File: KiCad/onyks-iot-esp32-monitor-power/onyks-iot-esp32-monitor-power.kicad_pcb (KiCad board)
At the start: 2 copper layers, 54.9 x 72.1 mm, 54 parts, among them J1 Uart_con, J10 PAD, J11 PAD, J12 PAD, J13 PAD, J14 +3V3_PAD, J15 +5V_PAD, J16 FOUT_conn, J17 Ground, J2 Jtag_con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

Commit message: fab files v1
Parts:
- added C9: 10u, Capacitor_SMD:C_0805_2012Metric, F.Cu at (160.1, 71.1)
- added D4: D_Zener, Diode_SMD:D_0805_2012Metric, F.Cu at (156.5, 73.4)
- added D5: D_Zener, Diode_SMD:D_0805_2012Metric, F.Cu at (152.9, 73.4)
- added R2: calc, Resistor_SMD:R_0805_2012Metric, F.Cu at (157.7, 67.1)
- added R3: calc, Resistor_SMD:R_0805_2012Metric, F.Cu at (157.7, 69.1)
- added R4: 1k, Resistor_SMD:R_0805_2012Metric, F.Cu at (156.4, 71.1)
- C1, C4, C6: value 100n -> 100n/10V
- C2: value 10u -> 10u/10V
- C3: value 1u -> 1u/10V
- C5: value 1n -> 1n/10V
- C7, C8: value 10u -> 10u/25V
- T1: value Transformer_1P_1S -> 2mA-2mA transformer
- moved J10 6.10 mm to (157.7, 64.4)
- moved J11 5.91 mm to (158.8, 62.5)
- moved J5 0.08 mm to (177.0, 106.3)
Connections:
- net SCL renamed /SCL
- net SDA renamed /SDA
- R10 pad 1: /A1 -> Net-(T1-SB)
- T1 pad 4: /A1 -> Net-(T1-SB)
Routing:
- net +3V3: track 199.0 -> 210.3 mm
- net Net-(T1-SB): track 0.00 -> 8.47 mm
- net /A1: track 20.2 -> 16.0 mm
- net /A0: track 35.6 -> 33.4 mm
- net /EN: track 99.6 -> 101.5 mm
- net Net-(C9-Pad2): track 0.00 -> 1.78 mm
- net Net-(D4-K): track 0.00 -> 1.78 mm
- net /SDA: track 40.4 -> 38.7 mm
- net /SCL: track 42.8 -> 41.2 mm
- net GND: vias 123 -> 70
- net Earth: vias 132 -> 55
- net (no net): vias 0 -> 3
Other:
- board text added: "ONYKS iot esp32 moitor power V1"
- board text removed: "ONYKS iot esp32 moitor power"

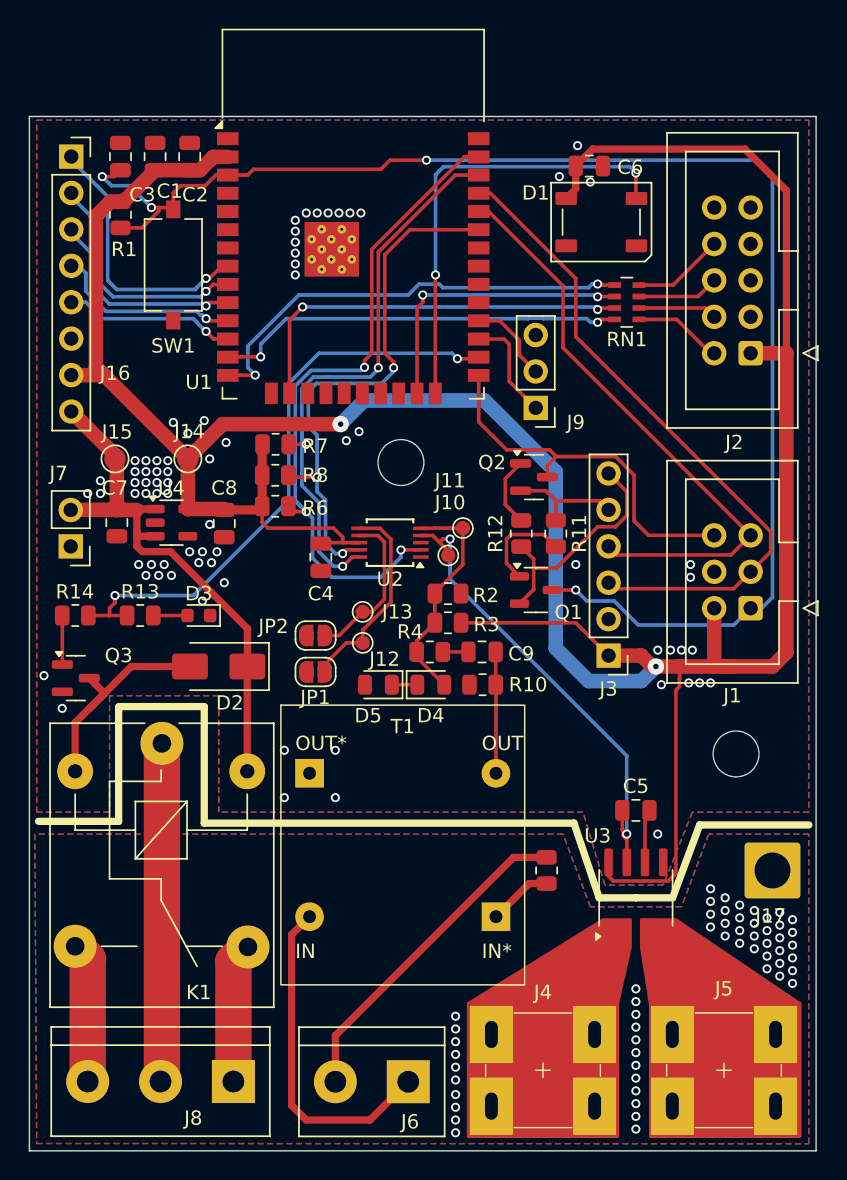
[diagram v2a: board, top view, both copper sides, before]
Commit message: vias 31mils
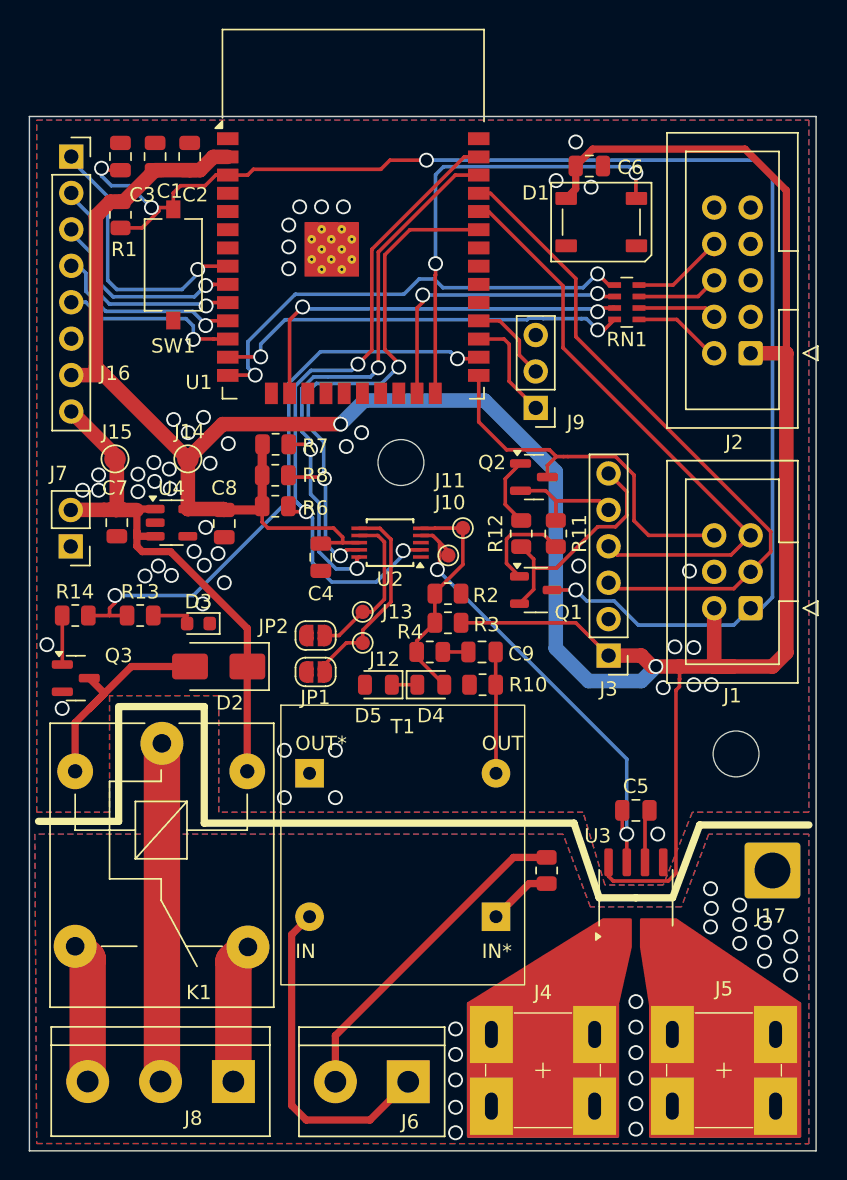
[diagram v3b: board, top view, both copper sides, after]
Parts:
- moved D3 0.56 mm to (140.3, 69.1)
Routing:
- net Net-(RN1D-R4.2): track 31.8 -> 32.8 mm
- net /SCL: track 41.2 -> 41.9 mm
- net /A0: track 33.4 -> 32.8 mm
- net /FOUT5: track 12.3 -> 12.8 mm
- net Net-(RN1A-R1.2): track 28.8 -> 29.4 mm
- net /EN: track 101.5 -> 102.1 mm
- net GND: vias 70 -> 45
- net Earth: vias 55 -> 23
